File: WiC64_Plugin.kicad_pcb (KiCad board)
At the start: 2 copper layers, 54.4 x 63.7 mm, 59 parts, among them CN1 USERPORT-C64, Q1 BSS138, Q10 BSS138, Q11 BSS138, Q2 BSS138, Q3 BSS138, Q4 BSS138, Q5 BSS138, Q6 BSS138, Q7 BSS138, Q8 BSS138, Q9 BSS138, SW1 RESET-C64, SW2 Function

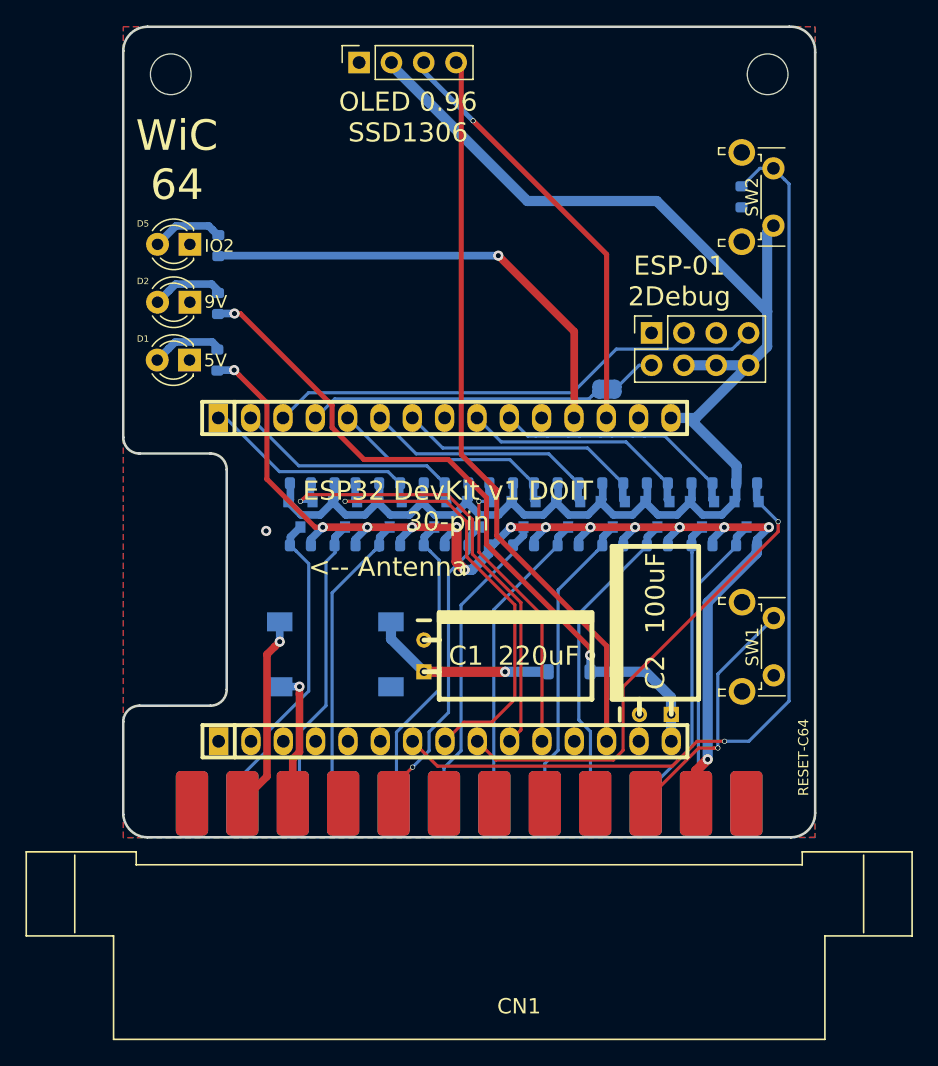
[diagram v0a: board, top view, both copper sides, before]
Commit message: Make all resistors 0805
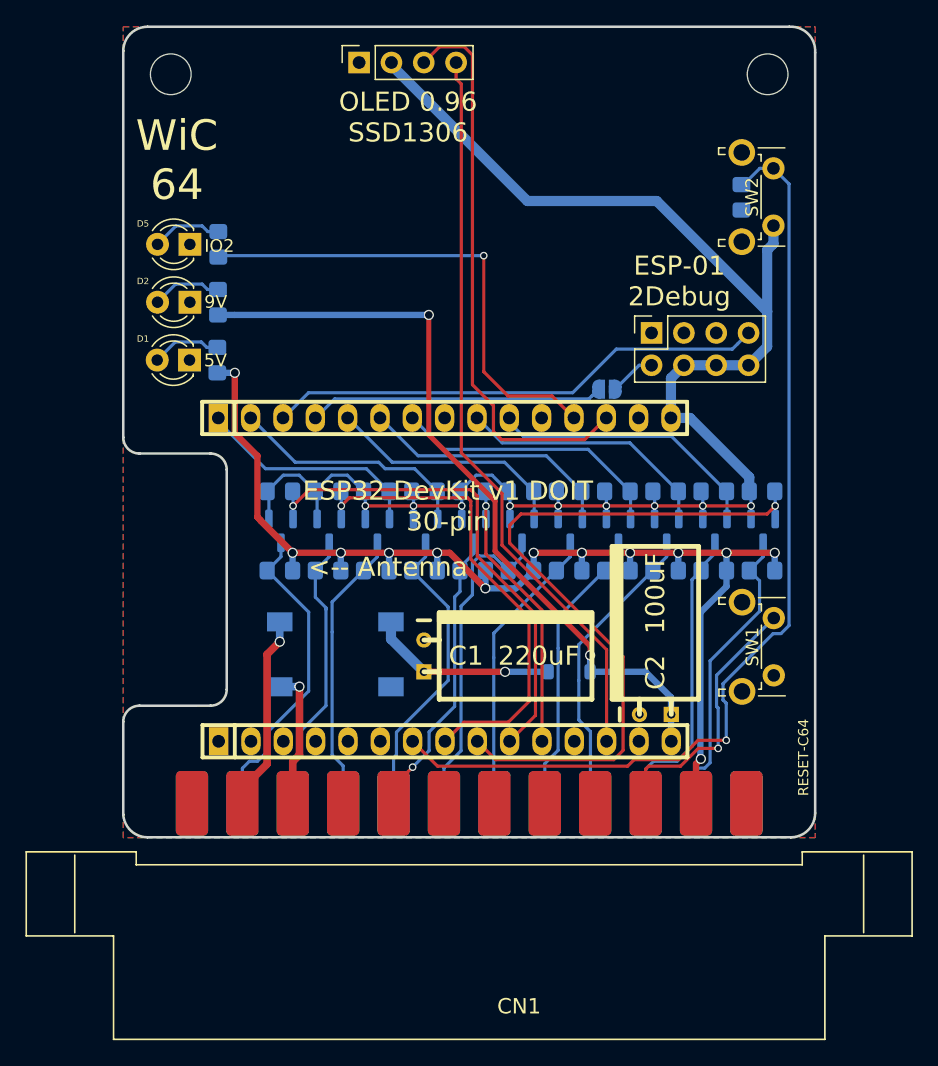
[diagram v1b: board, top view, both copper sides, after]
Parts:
- R1, R10, R11, R12, R13, R14, R15, R16, R17, R18, R19, R2, R20, R21, R22, R23, R24, R25, R26, R3, R4, R5, R6, R7, R8, R9: footprint Resistor_SMD:R_0603_1608Metric -> Resistor_SMD:R_0805_2012Metric_Pad1.20x1.40mm_HandSolder
- moved V4 4.41 mm to (166.8, 126.3)
- moved R22 2.56 mm to (134.5, 118.9)
- moved V3 2.49 mm to (148.8, 126.3)
- moved R20 2.39 mm to (138.3, 118.9)
- moved R2 2.32 mm to (172.4, 118.9)
- moved R18 2.24 mm to (142.1, 118.9)
- moved R4 2.19 mm to (168.6, 118.9)
- moved R16 2.12 mm to (145.8, 118.9)
- moved R6 2.08 mm to (164.8, 118.9)
- moved R14 2.04 mm to (149.6, 118.9)
- moved R8 2.01 mm to (161.0, 118.9)
- moved Q11 2.01 mm to (134.6, 115.8)
- moved R12 1.99 mm to (153.4, 118.9)
- moved R10 1.98 mm to (157.2, 118.9)
- moved Q1 1.84 mm to (172.4, 115.8)
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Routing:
- net /IO26: track 39.1 -> 57.4 mm
- net /SCL: track 34.1 -> 44.7 mm, vias 1 -> 0
- net /VIN: track 55.8 -> 60.5 mm
- net /IO25: track 35.0 -> 38.3 mm
- net /IO27: track 36.4 -> 39.3 mm
- net +3.3V: track 130.9 -> 133.7 mm, vias 0 -> 9
- net /IO16: track 19.5 -> 21.8 mm
- net /IO17: track 18.6 -> 20.4 mm
- net Net-(CN1-RESET): track 19.4 -> 21.2 mm
- net /PB4: track 24.1 -> 25.8 mm
- net /PB6: track 23.9 -> 22.3 mm
- net +5V: track 97.0 -> 95.4 mm, vias 14 -> 13
- net /IO18: track 20.1 -> 21.7 mm
- net /PC2: track 24.3 -> 22.9 mm
- net /IO2: track 37.2 -> 38.6 mm
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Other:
- board text added: "Rev. 0.6-Sukko"
- board text removed: "Rev. 0.6"

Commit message: Add 3D models
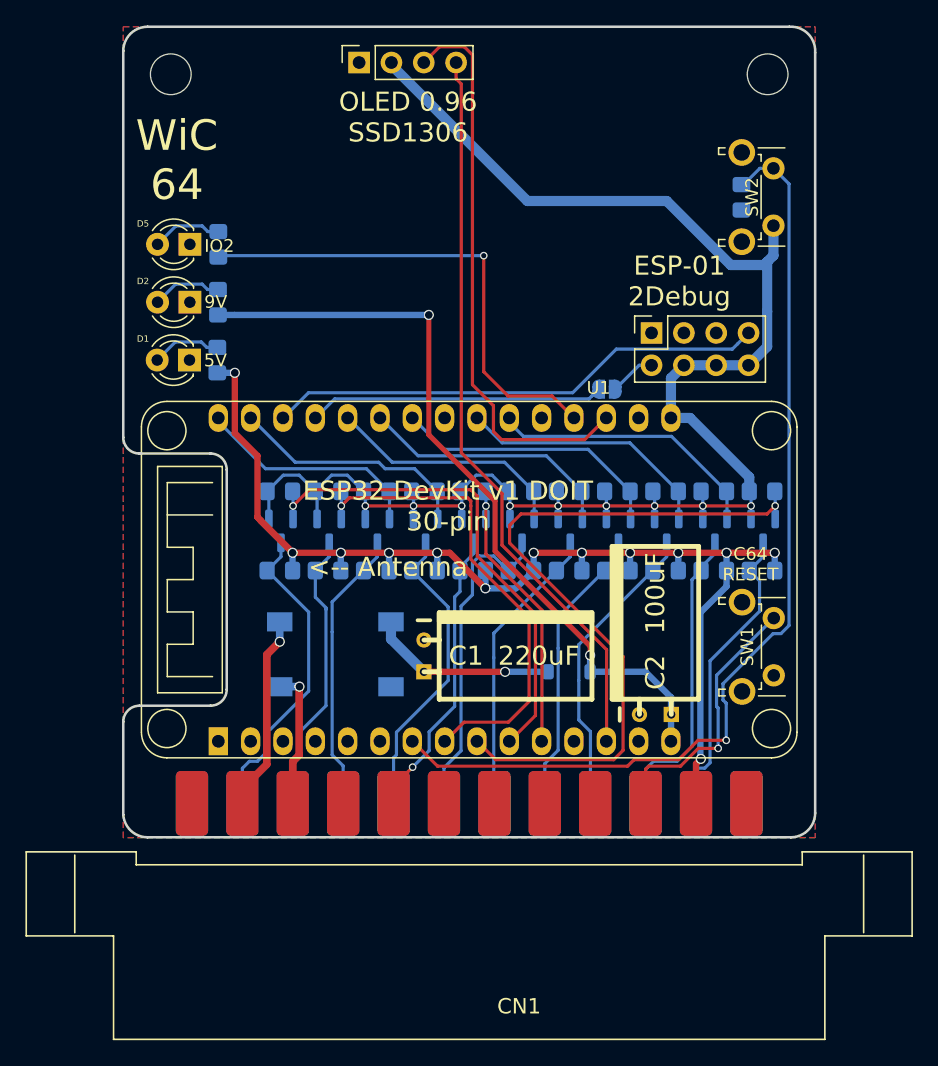
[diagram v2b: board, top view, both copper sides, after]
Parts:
- removed XU1-1, XU1-2: Conn_01x15_Female, w_pin_strip:pin_socket_15
- added U1: ESP32_DevKit_V1_DOIT, WiC64:esp32_devkit_v1_doit, F.Cu at (129.6, 119.6)
- CN2: renamed from XBrd1; value Conn_01x04_Female -> OLED0.96
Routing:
- net +3.3V: track 133.7 -> 132.3 mm
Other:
- board text added: "C64 RESET"

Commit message: Remove redundant symbols
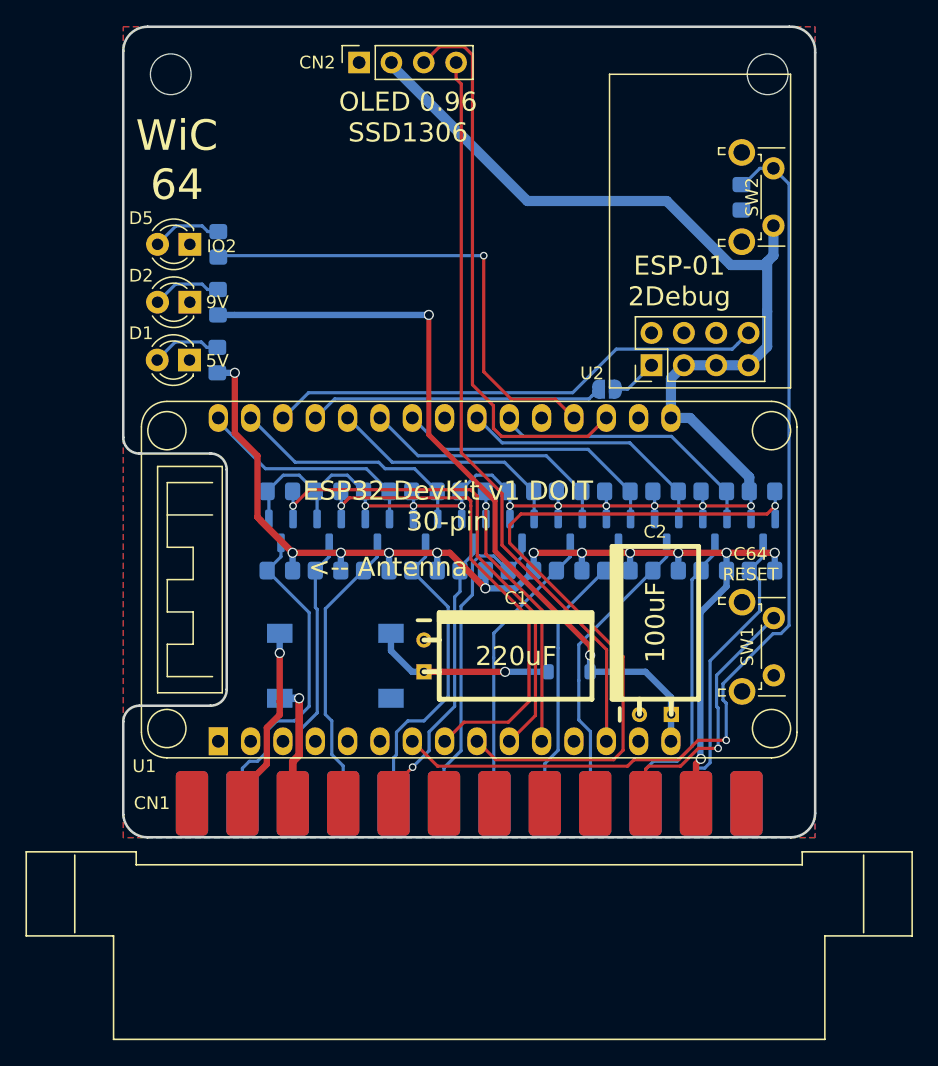
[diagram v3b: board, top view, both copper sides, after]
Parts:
- removed XU2: HEADER_4x2, Connector_PinSocket_2.54mm:PinSocket_2x04_P2.54mm_Vertical
- added U2: ESP-01_2x04, WiC64:ESP-01, F.Cu at (163.7, 102.8)
- moved D4 0.90 mm to (138.8, 126.4)
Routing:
- net Net-(CN1-9VAC1): track 10.8 -> 9.84 mm
- net Net-(CN1-9VAC2): track 15.3 -> 14.4 mm
- net /PA2: track 24.8 -> 25.6 mm
- net /PB5: track 23.9 -> 24.6 mm
- net /PB7: track 22.3 -> 21.8 mm
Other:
- board text added: "Original PCB-Design (C) 2021 by GMP"
- board text removed: "PCB-Design (C) 2021 by GMP"

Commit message: Allow powering ESP32 from 5V
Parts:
- added JP2: JMP_ESP_POWER, Jumper:SolderJumper-3_P1.3mm_Open_RoundedPad1.0x1.5mm, B.Cu at (153.4, 126.9)
- U2: value ESP-01_2x04 -> ESP-01
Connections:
- net /VIN renamed VCC
- C1 pad 1: Net-(D3-A) -> Net-(D4-+)
- D4 pad 1: Net-(D3-A) -> Net-(D4-+)
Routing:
- net Net-(D4-+): track 0.00 -> 12.8 mm, vias 0 -> 1
- net Net-(D3-A): track 14.4 -> 2.13 mm, vias 1 -> 0
- net +5V: track 95.4 -> 104.1 mm
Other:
- board text added: "5V"
- board text added: "9V"
